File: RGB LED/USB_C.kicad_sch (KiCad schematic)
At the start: 1 part, among them J1 USB_C_Receptacle_USB2.0_16P

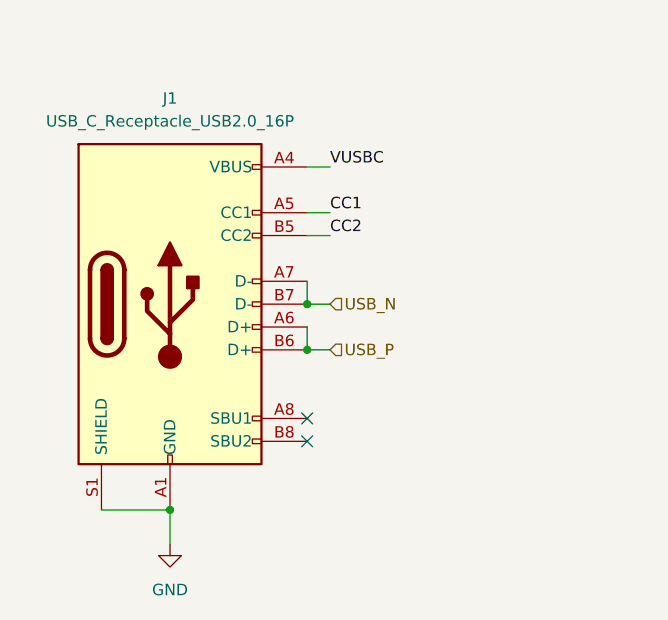
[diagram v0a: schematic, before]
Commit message: edited according to feedback
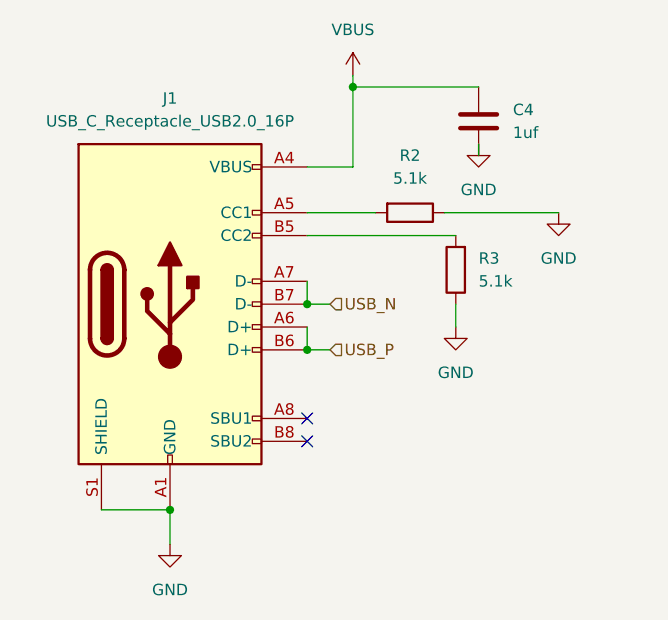
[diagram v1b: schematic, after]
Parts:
- added C4: 1uf, symbol Device:C
- added R2, R3: 5.1k, symbol Device:R
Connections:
- net GND: now also C4.2, R2.1, R3.1
- net CC1: no longer names the net of J1.A5 (CC1)
- net CC1: now also R2.2
- net CC2: no longer names the net of J1.B5 (CC2)
- net CC2: now also R3.2
- net VUSBC renamed VBUS
- net VBUS: now also C4.1
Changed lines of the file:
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@@
 (kicad_sch (version 20230121) (generator eeschema)
   (paper "A4")
+  (junction (at 104.14 52.07) (diameter 0) (color 0 0 0 0)
+  )
   (junction (at 83.82 99.06) (diameter 0) (color 0 0 0 0)
   )
@@
     (stroke (width 0) (type default))
   )
-  (wire (pts (xy 99.06 66.04) (xy 101.6 66.04))
+  (wire (pts (xy 115.57 76.2) (xy 115.57 78.74))
+    (stroke (width 0) (type default))
+  )
+  (wire (pts (xy 104.14 52.07) (xy 118.11 52.07))
+    (stroke (width 0) (type default))
+  )
+  (wire (pts (xy 99.06 66.04) (xy 106.68 66.04))
     (stroke (width 0) (type default))
   )
@@
     (stroke (width 0) (type default))
   )
+  (wire (pts (xy 118.11 59.69) (xy 118.11 58.42))
+    (stroke (width 0) (type default))
+  )
   (wire (pts (xy 76.2 99.06) (xy 83.82 99.06))
     (stroke (width 0) (type default))
   )
-  (wire (pts (xy 99.06 68.58) (xy 101.6 68.58))
+  (wire (pts (xy 114.3 66.04) (xy 127 66.04))
     (stroke (width 0) (type default))
   )
@@
     (stroke (width 0) (type default))
   )
-  (wire (pts (xy 99.06 60.96) (xy 101.6 60.96))
-    (stroke (width 0) (type default))
-  )
-  (label "CC2" (at 101.6 68.58 0) (fields_autoplaced)
-    (effects (font (size 1.27 1.27)) (justify left bottom))
-  )
-  (label "CC1" (at 101.6 66.04 0) (fields_autoplaced)
-    (effects (font (size 1.27 1.27)) (justify left bottom))
-  )
-  (label "VUSBC" (at 101.6 60.96 0) (fields_autoplaced)
-    (effects (font (size 1.27 1.27)) (justify left bottom))
+  (wire (pts (xy 104.14 52.07) (xy 104.14 60.96))
+    (stroke (width 0) (type default))
+  )
+  (wire (pts (xy 104.14 60.96) (xy 99.06 60.96))
+    (stroke (width 0) (type default))
+  )
+  (wire (pts (xy 99.06 68.58) (xy 115.57 68.58))
+    (stroke (width 0) (type default))
+  )
+  (wire (pts (xy 104.14 50.8) (xy 104.14 52.07))
+    (stroke (width 0) (type default))
   )
   (hierarchical_label "USB_N" (shape input) (at 101.6 76.2 0) (fields_autoplaced)
@@
   (hierarchical_label "USB_P" (shape input) (at 101.6 81.28 0) (fields_autoplaced)
     (effects (font (size 1.27 1.27)) (justify left))
+  )
+  (symbol (lib_id "power:VBUS") (at 104.14 50.8 0) (unit 1)
+    (in_bom yes) (on_board yes) (dnp no)
+    (property "Reference" "#PWR014" (at 104.14 54.61 0)
+      (effects (font (size 1.27 1.27)) hide)
+    )
+    (property "Value" "VBUS" (at 104.14 45.72 0)
+      (effects (font (size 1.27 1.27)))
+    )
+    (property "Footprint" "" (at 104.14 50.8 0)
+      (effects (font (size 1.27 1.27)) hide)
+    )
+    (property "Datasheet" "" (at 104.14 50.8 0)
+      (effects (font (size 1.27 1.27)) hide)
+    )
+    (pin "1")
+    (instances
+      (project "RGB LED"
+        (path "/ac9a3c3e-b738-422c-8f43-94adc2643155/bd384384-9f9f-4085-9b6e-b3cdc5789f67"
+          (reference "#PWR014") (unit 1)
+        )
+      )
+    )
   )
   (symbol (lib_id "Connector:USB_C_Receptacle_USB2.0_16P") (at 83.82 76.2 0) (unit 1)
@@
         )
       )
+    )
+  )
+  (symbol (lib_id "Device:C") (at 118.11 55.88 0) (unit 1)
+    (in_bom yes) (on_board yes) (dnp no) (fields_autoplaced)
+    (property "Reference" "C4" (at 121.92 54.61 0)
+      (effects (font (size 1.27 1.27)) (justify left))
+    )
+    (property "Value" "1uf" (at 121.92 57.15 0)
+      (effects (font (size 1.27 1.27)) (justify left))
+    )
+    (property "Footprint" "" (at 119.0752 59.69 0)
+      (effects (font (size 1.27 1.27)) hide)
+    )
+    (property "Datasheet" "~" (at 118.11 55.88 0)
+      (effects (font (size 1.27 1.27)) hide)
+    )
+    (pin "1")
+    (pin "2")
+    (instances
+      (project "RGB LED"
+        (path "/ac9a3c3e-b738-422c-8f43-94adc2643155/bd384384-9f9f-4085-9b6e-b3cdc5789f67"
+          (reference "C4") (unit 1)
+        )
+      )
+    )
+  )
+  (symbol (lib_id "power:GND") (at 118.11 58.42 0) (unit 1)
+    (in_bom yes) (on_board yes) (dnp no) (fields_autoplaced)
+    (property "Reference" "#PWR013" (at 118.11 64.77 0)
+      (effects (font (size 1.27 1.27)) hide)
+    )
+    (property "Value" "GND" (at 118.11 63.5 0)
+      (effects (font (size 1.27 1.27)))
+    )
+    (property "Footprint" "" (at 118.11 58.42 0)
+      (effects (font (size 1.27 1.27)) hide)
+    )
+    (property "Datasheet" "" (at 118.11 58.42 0)
+      (effects (font (size 1.27 1.27)) hide)
+    )
+    (pin "1")
+    (instances
+      (project "RGB LED"
+        (path "/ac9a3c3e-b738-422c-8f43-94adc2643155/bd384384-9f9f-4085-9b6e-b3cdc5789f67"
+          (reference "#PWR013") (unit 1)
+        )
+      )
+    )
+  )
+  (symbol (lib_id "Device:R") (at 110.49 66.04 270) (unit 1)
+    (in_bom yes) (on_board yes) (dnp no) (fields_autoplaced)
+    (property "Reference" "R2" (at 110.49 59.69 90)
+      (effects (font (size 1.27 1.27)))
+    )
+    (property "Value" "5.1k" (at 110.49 62.23 90)
+      (effects (font (size 1.27 1.27)))
+    )
+    (property "Footprint" "" (at 110.49 64.262 90)
+      (effects (font (size 1.27 1.27)) hide)
+    )
+    (property "Datasheet" "~" (at 110.49 66.04 0)
+      (effects (font (size 1.27 1.27)) hide)
+    )
+    (pin "2")
+    (pin "1")
+    (instances
+      (project "RGB LED"
+        (path "/ac9a3c3e-b738-422c-8f43-94adc2643155/bd384384-9f9f-4085-9b6e-b3cdc5789f67"
+          (reference "R2") (unit 1)
+        )
+      )
+    )
+  )
+  (symbol (lib_id "power:GND") (at 115.57 78.74 0) (unit 1)
+    (in_bom yes) (on_board yes) (dnp no) (fields_autoplaced)
+    (property "Reference" "#PWR020" (at 115.57 85.09 0)
+      (effects (font (size 1.27 1.27)) hide)
+    )
+    (property "Value" "GND" (at 115.57 83.82 0)
+      (effects (font (size 1.27 1.27)))
+    )
+    (property "Footprint" "" (at 115.57 78.74 0)
+      (effects (font (size 1.27 1.27)) hide)
+    )
+    (property "Datasheet" "" (at 115.57 78.74 0)
+      (effects (font (size 1.27 1.27)) hide)
+    )
+    (pin "1")
+    (instances
+      (project "RGB LED"
+        (path "/ac9a3c3e-b738-422c-8f43-94adc2643155/bd384384-9f9f-4085-9b6e-b3cdc5789f67"
+          (reference "#PWR020") (unit 1)
+        )
+      )
+    )
+  )
+  (symbol (lib_id "power:GND") (at 127 66.04 0) (unit 1)
+    (in_bom yes) (on_board yes) (dnp no) (fields_autoplaced)
+    (property "Reference" "#PWR019" (at 127 72.39 0)
+      (effects (font (size 1.27 1.27)) hide)
+    )
+    (property "Value" "GND" (at 127 71.12 0)
+      (effects (font (size 1.27 1.27)))
+    )
+    (property "Footprint" "" (at 127 66.04 0)
+      (effects (font (size 1.27 1.27)) hide)
+    )
+    (property "Datasheet" "" (at 127 66.04 0)
+      (effects (font (size 1.27 1.27)) hide)
+    )
+    (pin "1")
+    (instances
+      (project "RGB LED"
+        (path "/ac9a3c3e-b738-422c-8f43-94adc2643155/bd384384-9f9f-4085-9b6e-b3cdc5789f67"
+          (reference "#PWR019") (unit 1)
+        )
+      )
+    )
+  )
+  (symbol (lib_id "Device:R") (at 115.57 72.39 180) (unit 1)
+    (in_bom yes) (on_board yes) (dnp no) (fields_autoplaced)
+    (property "Reference" "R3" (at 118.11 71.12 0)
+      (effects (font (size 1.27 1.27)) (justify right))
+    )
+    (property "Value" "5.1k" (at 118.11 73.66 0)
+      (effects (font (size 1.27 1.27)) (justify right))
+    )
+    (property "Footprint" "" (at 117.348 72.39 90)
+      (effects (font (size 1.27 1.27)) hide)
+    )
+    (property "Datasheet" "~" (at 115.57 72.39 0)
+      (effects (font (size 1.27 1.27)) hide)
+    )
+    (pin "2")
+    (pin "1")
+    (instances
+      (project "RGB LED"
+        (path "/ac9a3c3e-b738-422c-8f43-94adc2643155/bd384384-9f9f-4085-9b6e-b3cdc5789f67"
+          (reference "R3") (unit 1)
+        )
+      )

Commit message: added footprints
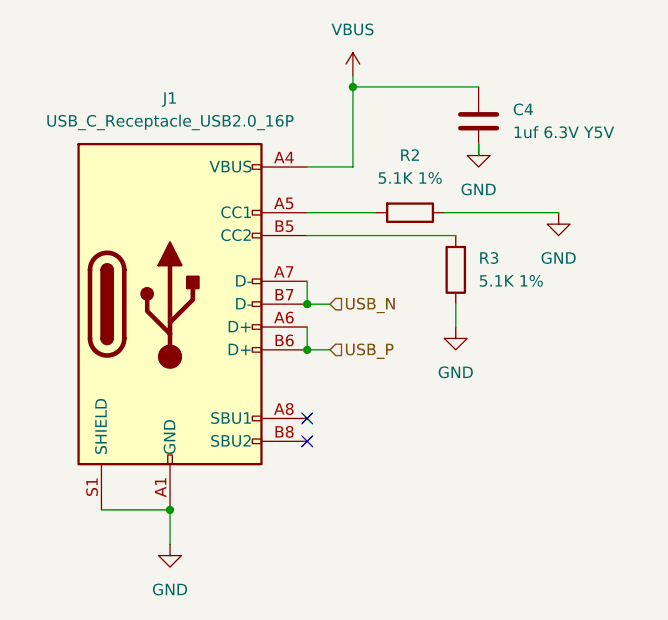
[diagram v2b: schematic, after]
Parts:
- C4: value 1uf -> 1uf 6.3V Y5V; footprint (none) -> Capacitor_SMD:C_0603_1608Metric
- J1: footprint (none) -> Library:GCT_USB4085-GF-A_REVB
- R2, R3: value 5.1k -> 5.1K 1%; footprint (none) -> Resistor_SMD:R_0603_1608Metric
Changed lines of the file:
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@@
       (effects (font (size 1.27 1.27)))
     )
-    (property "Footprint" "" (at 87.63 76.2 0)
+    (property "Footprint" "Library:GCT_USB4085-GF-A_REVB" (at 87.63 76.2 0)
       (effects (font (size 1.27 1.27)) hide)
     )
@@
       (effects (font (size 1.27 1.27)) (justify left))
     )
-    (property "Value" "1uf" (at 121.92 57.15 0)
+    (property "Value" "1uf 6.3V Y5V" (at 121.92 57.15 0)
       (effects (font (size 1.27 1.27)) (justify left))
     )
-    (property "Footprint" "" (at 119.0752 59.69 0)
+    (property "Footprint" "Capacitor_SMD:C_0603_1608Metric" (at 119.0752 59.69 0)
       (effects (font (size 1.27 1.27)) hide)
     )
@@
       (effects (font (size 1.27 1.27)))
     )
-    (property "Value" "5.1k" (at 110.49 62.23 90)
+    (property "Value" "5.1K 1%" (at 110.49 62.23 90)
       (effects (font (size 1.27 1.27)))
     )
-    (property "Footprint" "" (at 110.49 64.262 90)
+    (property "Footprint" "Resistor_SMD:R_0603_1608Metric" (at 110.49 64.262 90)
       (effects (font (size 1.27 1.27)) hide)
     )
@@
       (effects (font (size 1.27 1.27)) (justify right))
     )
-    (property "Value" "5.1k" (at 118.11 73.66 0)
+    (property "Value" "5.1K 1%" (at 118.11 73.66 0)
       (effects (font (size 1.27 1.27)) (justify right))
     )
-    (property "Footprint" "" (at 117.348 72.39 90)
+    (property "Footprint" "Resistor_SMD:R_0603_1608Metric" (at 117.348 72.39 90)
       (effects (font (size 1.27 1.27)) hide)
     )

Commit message: started layout
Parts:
- C4: value 1uf 6.3V Y5V -> 1uF 6.3V Y5V
- J1: footprint Library:GCT_USB4085-GF-A_REVB -> Connector_USB:USB_C_Receptacle_GCT_USB4085
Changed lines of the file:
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@@
       (effects (font (size 1.27 1.27)))
     )
-    (property "Footprint" "Library:GCT_USB4085-GF-A_REVB" (at 87.63 76.2 0)
+    (property "Footprint" "Connector_USB:USB_C_Receptacle_GCT_USB4085" (at 87.63 76.2 0)
       (effects (font (size 1.27 1.27)) hide)
     )
@@
       (effects (font (size 1.27 1.27)) (justify left))
     )
-    (property "Value" "1uf 6.3V Y5V" (at 121.92 57.15 0)
+    (property "Value" "1uF 6.3V Y5V" (at 121.92 57.15 0)
       (effects (font (size 1.27 1.27)) (justify left))
     )

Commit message: draft of layout
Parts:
- added TP2: TestPoint, TestPoint:TestPoint_Keystone_5015_Micro-Minature, symbol Connector:TestPoint
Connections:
- net VBUS: now also TP2.1
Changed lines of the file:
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@@
   (junction (at 99.06 81.28) (diameter 0) (color 0 0 0 0)
+  )
+  (junction (at 101.6 60.96) (diameter 0) (color 0 0 0 0)
   )
   (no_connect (at 99.06 88.9))
@@
     (stroke (width 0) (type default))
   )
+  (wire (pts (xy 101.6 60.96) (xy 99.06 60.96))
+    (stroke (width 0) (type default))
+  )
   (wire (pts (xy 118.11 59.69) (xy 118.11 58.42))
     (stroke (width 0) (type default))
@@
     (stroke (width 0) (type default))
   )
-  (wire (pts (xy 104.14 60.96) (xy 99.06 60.96))
+  (wire (pts (xy 104.14 60.96) (xy 101.6 60.96))
     (stroke (width 0) (type default))
   )
@@
         )
       )
+    )
+  )
+  (symbol (lib_id "Connector:TestPoint") (at 101.6 60.96 0) (unit 1)
+    (in_bom yes) (on_board yes) (dnp no) (fields_autoplaced)
+    (property "Reference" "TP2" (at 104.14 56.388 0)
+      (effects (font (size 1.27 1.27)) (justify left))
+    )
+    (property "Value" "TestPoint" (at 104.14 58.928 0)
+      (effects (font (size 1.27 1.27)) (justify left))
+    )
+    (property "Footprint" "TestPoint:TestPoint_Keystone_5015_Micro-Minature" (at 106.68 60.96 0)
+      (effects (font (size 1.27 1.27)) hide)
+    )
+    (property "Datasheet" "~" (at 106.68 60.96 0)
+      (effects (font (size 1.27 1.27)) hide)
+    )
+    (pin "1")
+    (instances
+      (project "RGB LED"
+        (path "/ac9a3c3e-b738-422c-8f43-94adc2643155/bd384384-9f9f-4085-9b6e-b3cdc5789f67"
+          (reference "TP2") (unit 1)
+        )
+      )
